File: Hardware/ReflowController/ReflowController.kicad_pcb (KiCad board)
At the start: 4 copper layers, 160 x 100 mm, 140 parts, among them J101 2060-1452, J102 2060-1452, J103 2060-1453, J104 2060-1452, J105 2060-1452, J106 2060-1452, J107 2060-1452, J108 2060-1452, J109 2060-1452, J110 2060-1452, J111 2060-1452, J112 2060-1452, J113 2060-1452, J114 2060-1452, J115 2060-1452, J201 nucleo_f042k6, J601 LCD_HEADER, Q601 BC848, SW601 RotaryEncoder_Switch, SW602 SW_UP, SW603 SW_DOWN, SW604 SW_LEFT, SW605 SW_RIGHT, SW606 SW_SELECT, SW607 SW_RET, SW608 SW_RESET, U301 TSR_1-2450, U302 LD1117S33TR_SOT223, U401 MAX31865xAP, U501 TB67H400AFNG, U601 PI4IOE5V6416, U701 VNQ5160K-E, U702 SZNUD3124DMT1G

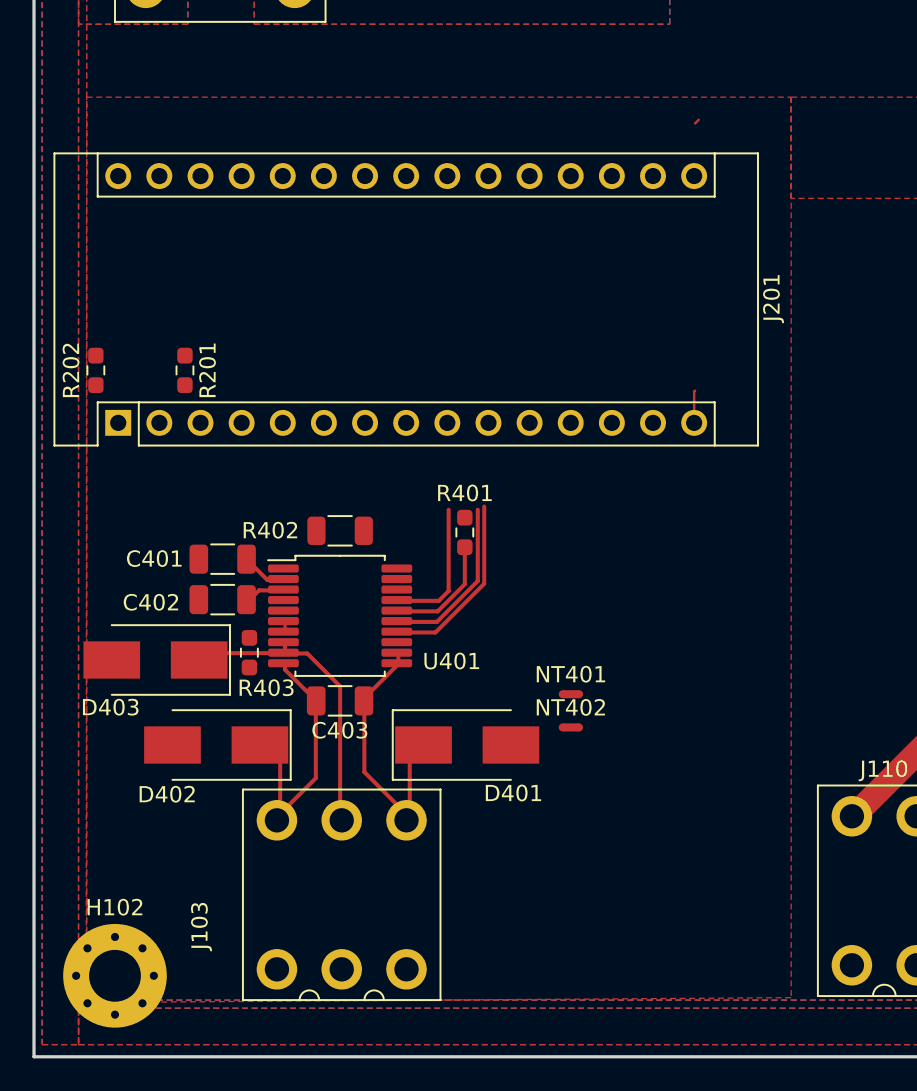
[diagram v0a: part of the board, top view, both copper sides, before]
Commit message: work on porttable and on layout of temperature sensor
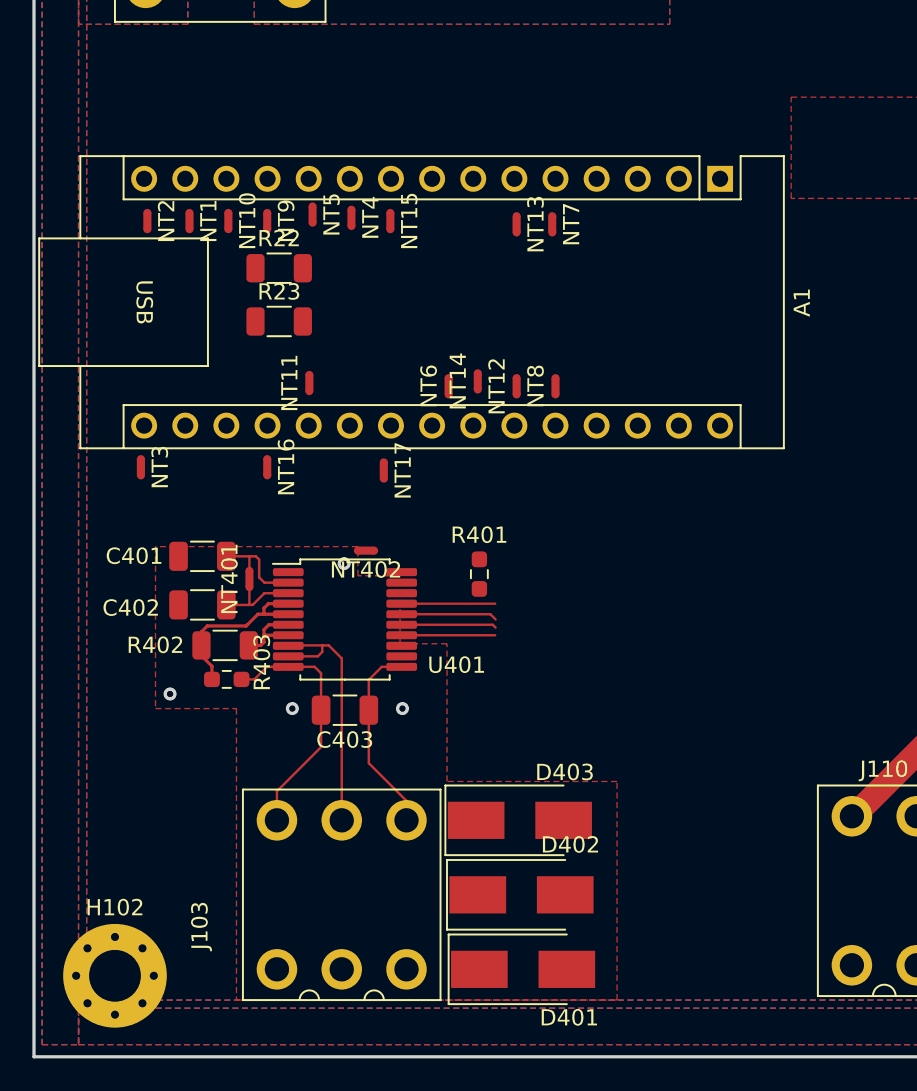
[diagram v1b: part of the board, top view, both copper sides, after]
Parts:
- removed J201: nucleo_f042k6, Module:Arduino_Nano
- removed R201, R202: 4.7K, Resistor_SMD:R_0603_1608Metric_Pad0.98x0.95mm_HandSolder
- added A1: NUCLEO_STM32F042K6, Module:Arduino_Nano, F.Cu at (109.4, 85.8)
- added NT1: NetTie_2, NetTie:NetTie-2_SMD_Pad0.5mm, F.Cu at (76.6, 88.4)
- added NT10: NetTie_2, NetTie:NetTie-2_SMD_Pad0.5mm, F.Cu at (79.0, 88.4)
- added NT11: NetTie_2, NetTie:NetTie-2_SMD_Pad0.5mm, F.Cu at (84.0, 98.4)
- added NT12: NetTie_2, NetTie:NetTie-2_SMD_Pad0.5mm, F.Cu at (96.8, 98.6)
- added NT13: NetTie_2, NetTie:NetTie-2_SMD_Pad0.5mm, F.Cu at (96.8, 88.6)
- added NT14: NetTie_2, NetTie:NetTie-2_SMD_Pad0.5mm, F.Cu at (94.4, 98.3)
- added NT15: NetTie_2, NetTie:NetTie-2_SMD_Pad0.5mm, F.Cu at (89.0, 88.4)
- added NT16: NetTie_2, NetTie:NetTie-2_SMD_Pad0.5mm, F.Cu at (81.4, 103.6)
- added NT17: NetTie_2, NetTie:NetTie-2_SMD_Pad0.5mm, F.Cu at (88.6, 103.8)
- added NT2: NetTie_2, NetTie:NetTie-2_SMD_Pad0.5mm, F.Cu at (74.0, 88.4)
- added NT3: NetTie_2, NetTie:NetTie-2_SMD_Pad0.5mm, F.Cu at (73.6, 103.6)
- added NT4: NetTie_2, NetTie:NetTie-2_SMD_Pad0.5mm, F.Cu at (86.6, 88.2)
- added NT5: NetTie_2, NetTie:NetTie-2_SMD_Pad0.5mm, F.Cu at (84.2, 88.0)
- added NT6: NetTie_2, NetTie:NetTie-2_SMD_Pad0.5mm, F.Cu at (92.6, 98.6)
- added NT7: NetTie_2, NetTie:NetTie-2_SMD_Pad0.5mm, F.Cu at (99.0, 88.6)
- added NT8: NetTie_2, NetTie:NetTie-2_SMD_Pad0.5mm, F.Cu at (99.2, 98.6)
- added NT9: NetTie_2, NetTie:NetTie-2_SMD_Pad0.5mm, F.Cu at (81.4, 88.4)
- added R22: 4k7, Resistor_SMD:R_1206_3216Metric, F.Cu at (82.1, 91.3)
- added R23: 4k7, Resistor_SMD:R_1206_3216Metric, F.Cu at (82.1, 94.6)
- moved D403 24.6 mm to (97.0, 125.4), turned to 0 degrees
- moved NT401 21.1 mm to (80.3, 110.5), turned to 90 degrees
- moved D402 21.0 mm to (97.1, 130.0), turned to 0 degrees
- moved NT402 16.7 mm to (87.5, 108.8), turned to 180 degrees
- moved D401 14.3 mm to (97.2, 134.6)
- moved R402 10.0 mm to (78.8, 114.6)
- moved R401 2.73 mm to (94.5, 110.2)
- moved R403 2.16 mm to (78.9, 116.7), turned to 180 degrees
- moved C402 1.29 mm to (77.4, 112.1)
- moved C401 1.26 mm to (77.4, 109.1)
- moved C403 0.65 mm to (86.2, 118.6)
- moved U401 0.37 mm to (86.2, 113.0)
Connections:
- J101 pad 2: /uC/PA2 -> /uC/~{INT_EMERGENCY_STOP}
- U601 pad 15: /ui/OI_AUX_1 -> /HSS_1_EN
- U601 pad 16: /ui/OI_AUX_2 -> /HSS_2_EN
- U601 pad 17: /ui/OI_AUX_3 -> /HSS_3_EN
- U601 pad 9: /ui/LED_INDICATION -> /HSS_4_EN
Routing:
- net /TemperatureReader/REFIN+: track 0.83 -> 11.0 mm
- net /MOSI: track 11.3 -> 5.77 mm
- net /TemperatureReader/PT100_-IN: track 16.8 -> 12.0 mm
- net /SCLK: track 10.3 -> 5.87 mm
- net /TemperatureReader/REFIN-: track 0.65 -> 4.93 mm
- net +3.3V: track 2.90 -> 6.04 mm
- net Net-(U401-VDD): track 2.48 -> 5.23 mm
- net /TemperatureReader/PT100_+OUT: track 18.9 -> 16.3 mm
- net /MISO: track 8.37 -> 5.77 mm
- net /BUZZER_PWM: track 47.6 -> 45.6 mm
- net /~{CS_TEMP}: track 7.08 -> 5.93 mm
- net /TemperatureReader/PT100_+IN: track 16.3 -> 15.6 mm
- net /TemperatureReader/T_AGND: vias 0 -> 4
- added copper zone on In2.Cu, net +3.3V
- added copper zone on F.Cu, net /TemperatureReader/T_AGND
- added copper zone on F.Cu, net GND
- added copper zone on In1.Cu, net GND
- removed copper zone on F.Cu, net +24V
- removed copper zone on In1.Cu, net /TemperatureReader/T_AGND
- removed copper zone on In1.Cu, net GNDPWR
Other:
- board text added: "http://www.elmac.co.uk/EMC_SelfStudy-std/Index.htm?context=380"
- board text added: "https://blog.upverter.com/2019/11/07/pcb-grounding-techniques-to-do-and-what-not-to-do/"

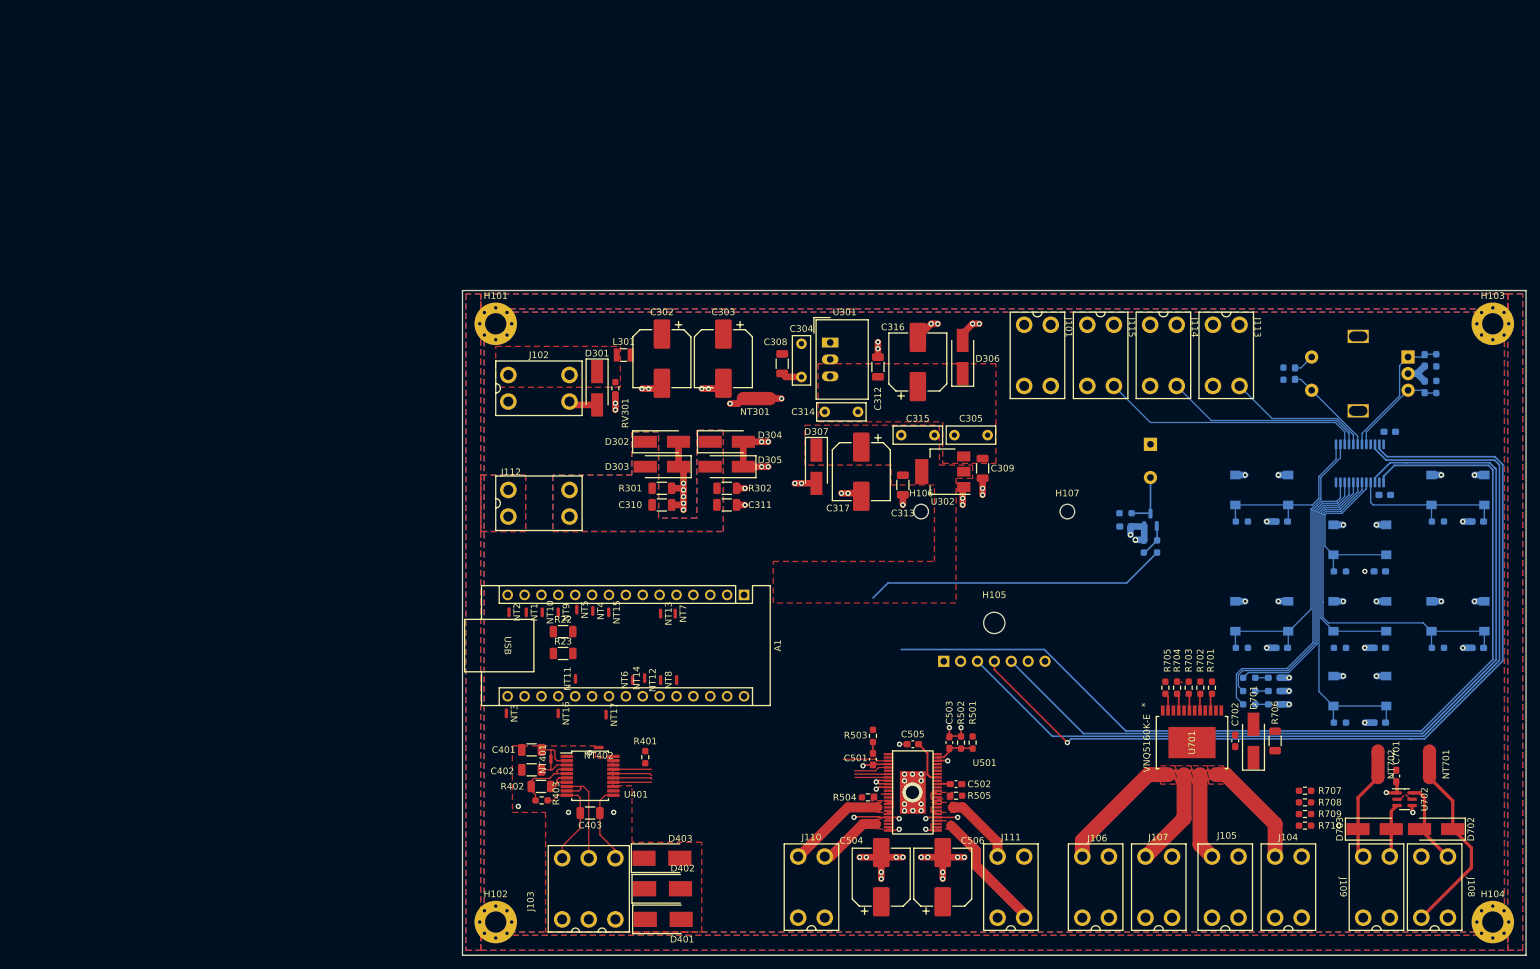
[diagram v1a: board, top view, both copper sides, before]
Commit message: work on layout of power
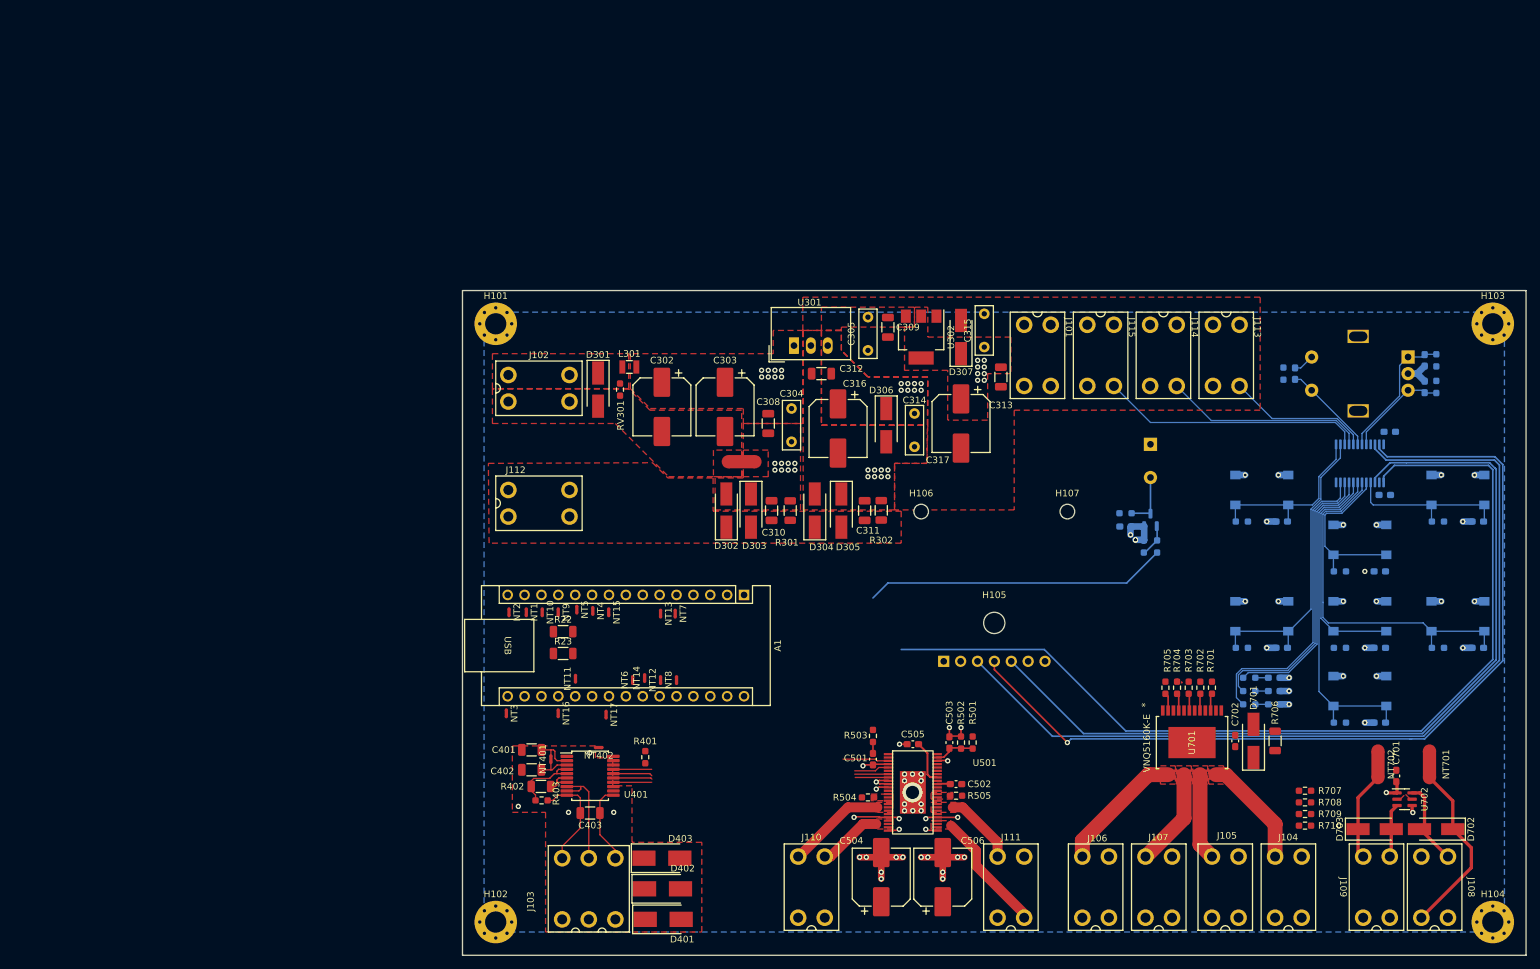
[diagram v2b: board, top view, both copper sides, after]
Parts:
- moved D307 29.2 mm to (142.0, 47.0), turned to 90 degrees
- moved C309 25.6 mm to (131.0, 45.5)
- moved C305 25.3 mm to (128.0, 44.0), turned to -90 degrees
- moved R302 23.5 mm to (130.0, 73.1), turned to -90 degrees
- moved C313 21.9 mm to (148.0, 53.0)
- moved C311 20.8 mm to (127.5, 73.1), turned to 90 degrees
- moved U302 20.5 mm to (136.0, 47.0), turned to -90 degrees
- moved R301 19.6 mm to (116.3, 73.1), turned to -90 degrees
- moved D305 18.5 mm to (124.0, 73.1), turned to -90 degrees
- moved C315 18.2 mm to (145.5, 48.5), turned to 90 degrees
- moved D304 16.8 mm to (120.0, 73.1), turned to 90 degrees
- moved C317 16.7 mm to (142.0, 60.0)
- moved C310 16.5 mm to (113.5, 73.1), turned to 90 degrees
- moved C316 15.6 mm to (123.5, 60.8), turned to -90 degrees
- moved D306 15.4 mm to (130.8, 60.2), turned to -90 degrees
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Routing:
- net GND: track 97.6 -> 60.9 mm, vias 53 -> 40
- net GNDPWR: track 64.5 -> 45.3 mm, vias 39 -> 41
- net /PSU/24V_GND_IN: track 15.9 -> 0.00 mm, vias 7 -> 0
- net +5V: vias 0 -> 8
- net +3.3V: vias 0 -> 8
- net +24V: vias 0 -> 8
- added copper zone on F.Cu, net +24V
- added copper zone on F.Cu, net /PSU/24V_GND_IN
- added copper zone on F.Cu, net GNDPWR
- removed copper zone on B.Cu, net Earth
- removed copper zone on In1.Cu, net Earth
- removed copper zone on In2.Cu, net Earth

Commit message: work on layout
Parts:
- moved L301 0.51 mm to (92.0, 51.0)
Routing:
- added copper zone on B.Cu, net GND
- removed copper zone on B.Cu, net +3.3V
- removed copper zone on In1.Cu, net /PSU/24V_GND_IN
- removed copper zone on In2.Cu, net GND
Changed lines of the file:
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@@
   )
   (footprint "020_SMD_Inductors:2520" (layer "F.Cu")
-    (at 92.1 51.5)
+    (at 92 51)
     (property "Sheetfile" "PSU.kicad_sch")
     (property "Sheetname" "PSU")
@@
     (property "man_no" "AVR-M1608C270KT6AB")
     (attr smd)
-    (fp_text reference "RV301" (at 3.9 -0.1 90) (layer "F.SilkS")
+    (fp_text reference "RV301" (at 6.1 1.7 -180) (layer "F.SilkS")
         (effects (font (size 1 1) (thickness 0.15)))
     )
@@
     (zone_connect 1)
     (attr smd)
-    (fp_text reference "J112" (at -3.5 -5 unlocked) (layer "F.SilkS")
+    (fp_text reference "J112" (at -0.5 -5 unlocked) (layer "F.SilkS")
         (effects (font (size 1 1) (thickness 0.15)))
     )
@@
         (xy 118.2 46)
         (xy 118.2 41)
-        (xy 187 41)
-        (xy 187 58)
+        (xy 150 41)
+        (xy 150 58)
         (xy 150 58)
         (xy 150 73)
@@
   )
   (zone (net 4) (net_name "/PSU/24V_GND_IN") (layer "F.Cu") (hatch edge 0.5)
-    (priority 8)
+    (priority 11)
     (connect_pads yes (clearance 0.2))
     (min_thickness 0.25) (filled_areas_thickness no)
@@
   )
   (zone (net 8) (net_name "GND") (layer "In1.Cu") (hatch edge 0.5)
-    (connect_pads (clearance 0.5))
+    (connect_pads (clearance 0.25))
     (min_thickness 0.25) (filled_areas_thickness no)
     (fill yes (thermal_gap 0.2) (thermal_bridge_width 0.5))
     (polygon
       (pts
-        (xy 70.25 43.25)
-        (xy 223.75 43.25)
+        (xy 70.25 78)
+        (xy 126 78)
+        (xy 126 65)
+        (xy 150 65)
+        (xy 150 43)
+        (xy 224 43)
         (xy 223.75 136.5)
         (xy 70.25 136.5)
@@
     )
   )
-  (zone (net 4) (net_name "/PSU/24V_GND_IN") (layer "In1.Cu") (hatch edge 0.5)
-    (priority 2)
-    (connect_pads yes (clearance 0.05))
-    (min_thickness 0.25) (filled_areas_thickness no)
-    (fill yes (thermal_gap 0.5) (thermal_bridge_width 0.5))
-    (polygon
-      (pts
-        (xy 72 51.25)
-        (xy 110.25 51.25)
-        (xy 110.25 57.25)
-        (xy 72 57.25)
-      )
-    )
-  )
   (zone (net 1) (net_name "+3.3V") (layer "In2.Cu") (name "T_AGND") (hatch edge 0.5)
     (priority 5)
@@
     )
   )
-  (zone (net 8) (net_name "GND") (layer "In2.Cu") (hatch edge 0.5)
-    (connect_pads (clearance 0.5))
-    (min_thickness 0.25) (filled_areas_thickness no)
-    (fill yes (thermal_gap 0.2) (thermal_bridge_width 0.5))
-    (polygon
-      (pts
-        (xy 70.25 43.25)
-        (xy 223.75 43.25)
-        (xy 223.75 136.5)
-        (xy 70.25 136.5)
-      )
-    )
-  )
-  (zone (net 1) (net_name "+3.3V") (layer "B.Cu") (hatch edge 0.5)
+  (zone (net 8) (net_name "GND") (layer "B.Cu") (hatch edge 0.5)
     (connect_pads (clearance 0.25))
     (min_thickness 0.25) (filled_areas_thickness no)
@@
     (polygon
       (pts
-        (xy 70.25 43.25)
-        (xy 223.75 43.25)
+        (xy 70.25 78)
+        (xy 126 78)
+        (xy 126 65)
+        (xy 150 65)
+        (xy 150 43)
+        (xy 224 43)
         (xy 223.75 136.5)
         (xy 70.25 136.5)

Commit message: Started layout with Edwin
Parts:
- removed D603: BLUE, LED_SMD:LED_0603_1608Metric_Pad1.05x0.95mm_HandSolder
- removed J113, J114, J115: 2060-1452, 810_connectors_clable_to_Board:wago_2060-1452
- removed R606: 4.7K, Resistor_SMD:R_0603_1608Metric_Pad0.98x0.95mm_HandSolder
- NT4, NT5: moved to B.Cu
- moved C602 45.5 mm to (166.2, 82.5), turned to 180 degrees
- moved U601 38.6 mm to (170.0, 87.5), turned to 180 degrees
- moved C601 33.2 mm to (175.5, 84.5)
- moved NT1 16.1 mm to (72.8, 104.0)
- moved NT2 15.6 mm to (75.0, 104.0)
- moved R23 14.3 mm to (89.2, 82.2), turned to -90 degrees
- moved R22 9.95 mm to (86.2, 82.2), turned to -90 degrees
- moved NT5 5.54 mm to (87.8, 83.8), turned to 90 degrees
- moved NT4 4.45 mm to (86.5, 83.8), turned to 90 degrees
- moved R401 2.96 mm to (93.0, 112.8), turned to 0 degrees
- moved J101 2.50 mm to (156.0, 49.8)
- moved NT15 0.90 mm to (89.0, 87.5)
- moved NT17 0.45 mm to (89.0, 104.0)
- moved NT3 0.43 mm to (73.8, 104.0)
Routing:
- net /~{IO_INT}: track 145.4 -> 0.00 mm
- net /~{UI_RESET}: track 131.0 -> 0.00 mm
- net /SCL: track 137.7 -> 91.5 mm
- net /ui/LED_ERROR: track 45.6 -> 0.00 mm
- net /BUZZER_PWM: track 45.6 -> 0.00 mm
- net /SDA: track 137.6 -> 92.2 mm, vias 1 -> 0
- net /ui/LED_ALIVE: track 43.6 -> 0.00 mm
- net /ui/BTN_RIGHT: track 54.4 -> 13.0 mm
- net /ui/LED_INDICATION: track 40.9 -> 0.00 mm
- net /ui/OI_AUX_1: track 39.5 -> 0.00 mm
- net /ui/BTN_UP: track 51.2 -> 13.1 mm
- net /ui/BTN_LEFT: track 44.5 -> 13.1 mm
- net /ui/OI_AUX_2: track 30.5 -> 0.00 mm
- net /ui/BTN_SELECT: track 35.2 -> 8.49 mm
- net /uC/PB4: track 0.00 -> 23.8 mm
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- added copper zone on B.Cu, net +3.3V
- added copper zone on In1.Cu, net /TemperatureReader/T_AGND

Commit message: work on the lyout
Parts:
- removed R403: 10M, Resistor_SMD:R_0603_1608Metric_Pad0.98x0.95mm_HandSolder
- NT16, NT17, R401: moved to B.Cu
- moved R401 12.0 mm to (84.4, 104.3), turned to 90 degrees
- moved C402 9.37 mm to (84.0, 118.8), turned to -90 degrees
- moved C401 9.05 mm to (80.5, 117.6)
- moved NT401 8.89 mm to (83.0, 119.0), turned to 180 degrees
- moved R402 8.66 mm to (86.4, 118.8), turned to 90 degrees
- moved C403 4.38 mm to (88.7, 122.2)
- moved NT2 4.17 mm to (70.8, 103.5)
- moved NT402 3.51 mm to (84.3, 110.2), turned to -90 degrees
- moved NT1 2.25 mm to (75.0, 103.5)
- moved U401 1.99 mm to (84.7, 111.8), turned to 90 degrees
- moved NT17 1.74 mm to (87.3, 103.5), turned to 180 degrees
- moved NT3 0.96 mm to (72.9, 103.5)
- moved NT16 0.07 mm to (81.5, 103.5)
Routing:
- net /TemperatureReader/PT100_+OUT: track 26.9 -> 10.8 mm
- net /TemperatureReader/PT100_+IN: track 29.9 -> 16.1 mm
- net /~{TMP_RDY}: track 0.00 -> 12.4 mm, vias 0 -> 1
- net /TemperatureReader/REFIN+: track 11.0 -> 0.00 mm
- net /TemperatureReader/PT100_-IN: track 16.5 -> 5.70 mm
- net /~{CS_TEMP}: track 11.9 -> 6.22 mm, vias 0 -> 1
- net /uC/PB4: track 23.8 -> 18.5 mm
- net /TemperatureReader/REFIN-: track 4.93 -> 0.00 mm
- net /MOSI: track 20.9 -> 16.4 mm
- net /SCLK: track 19.8 -> 16.0 mm
- net /uC/PA0: track 0.00 -> 2.03 mm
- net /uC/PB5: track 19.2 -> 17.8 mm
- net /MISO: track 18.3 -> 17.0 mm
- net /uC/PA4: track 2.49 -> 3.32 mm
- net Net-(U401-VDD): track 5.23 -> 4.45 mm
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- added copper zone on B.Cu, net /TemperatureReader/T_AGND
- added copper zone on In2.Cu, net /TemperatureReader/T_AGND
- added copper zone on In2.Cu, net GND
- added copper zone on In1.Cu, net GNDPWR
- added copper zone on In2.Cu, net GNDPWR
